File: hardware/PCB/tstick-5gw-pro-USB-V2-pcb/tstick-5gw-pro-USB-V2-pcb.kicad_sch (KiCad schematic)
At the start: 55 parts, among them J1 USB_C_Receptacle_USB2.0, J2 GPIO2, J3 GPIO1, Q3 BSS138, SW1 JST-SH-1.00mm 1x2, SW2 PTS810 SJM Switch, SW3 PTS810 SJM Switch, U1 max8819ceti+, U4 PCA9306DP

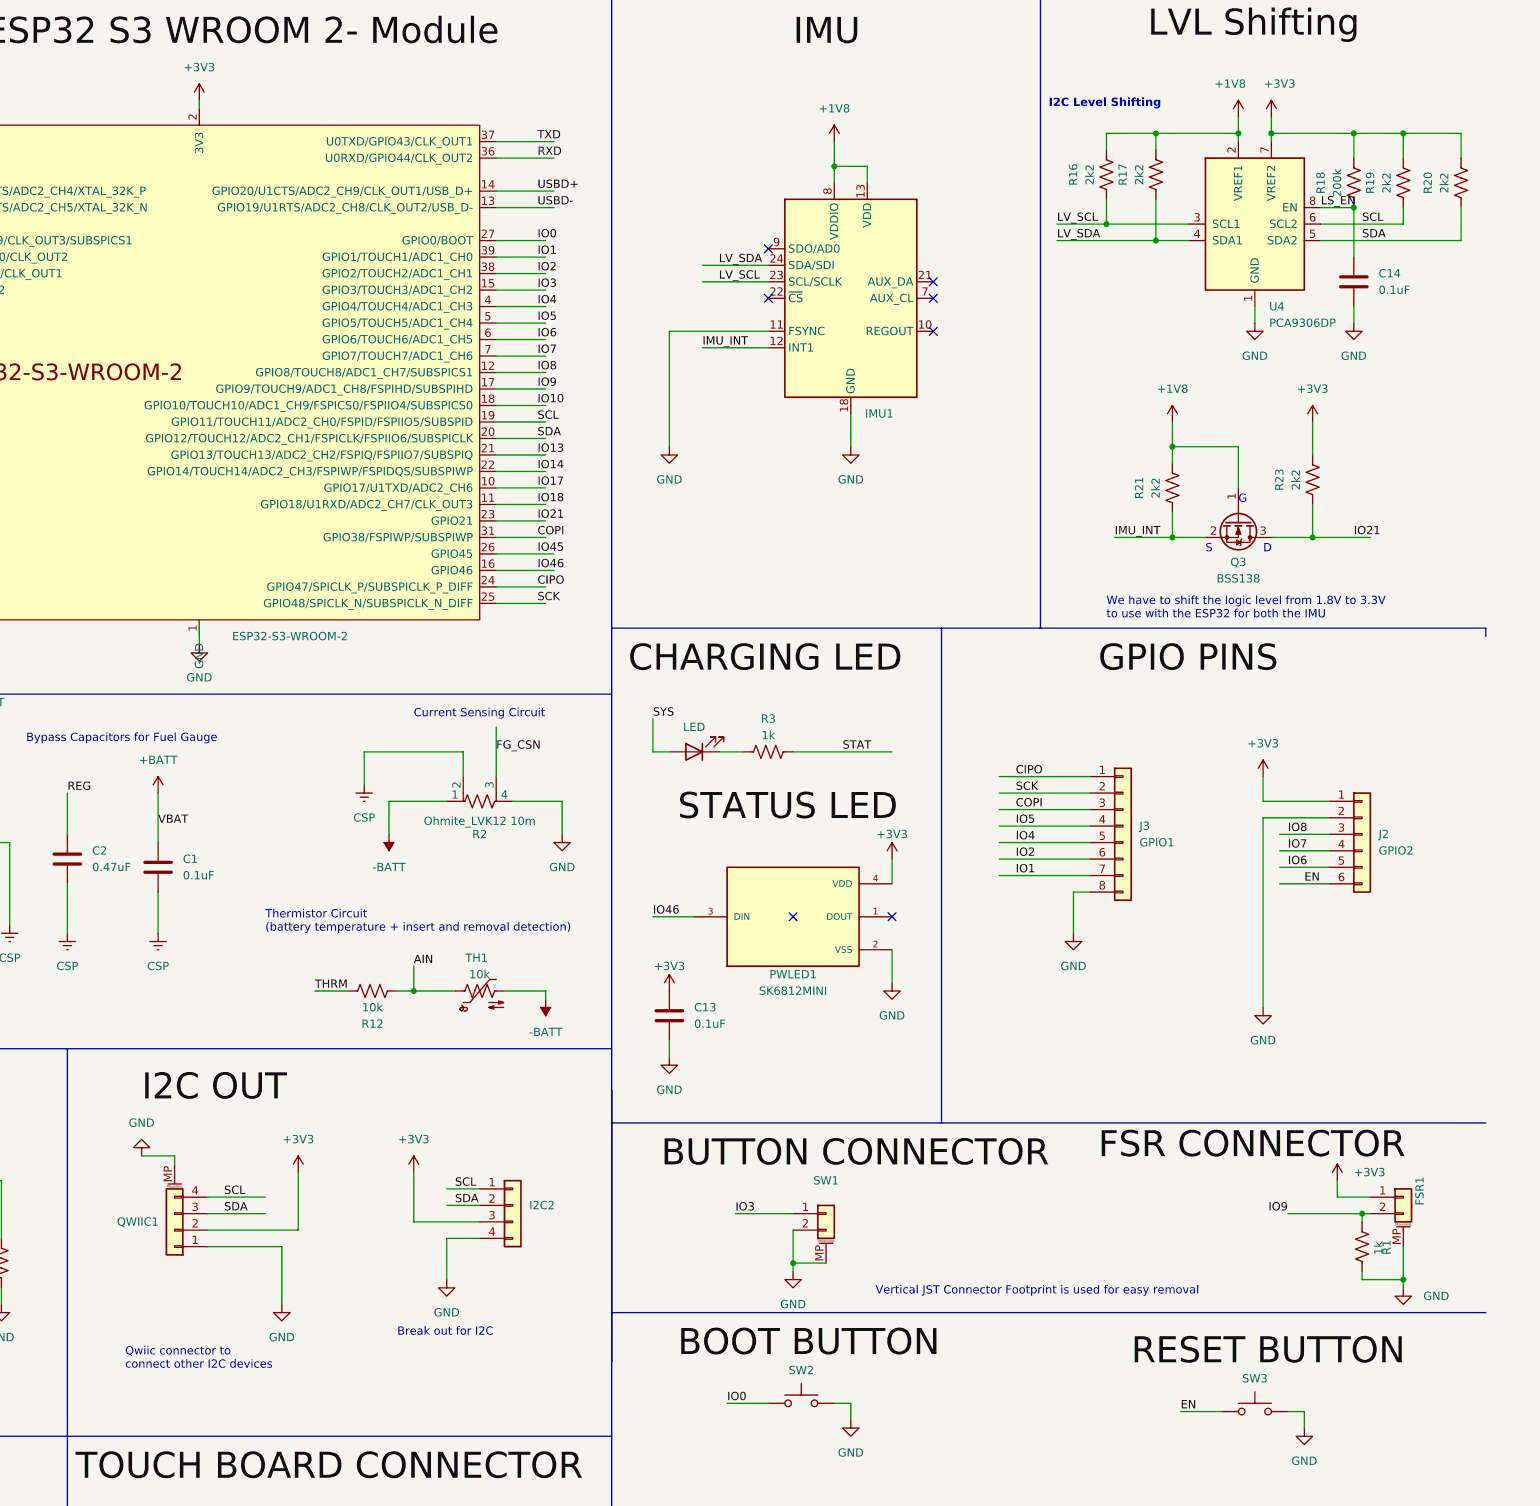
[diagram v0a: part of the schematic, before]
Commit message: cleaned up layout, board 1x2.2 inches, holes now 0.7 inch apart, lined up gpio holes
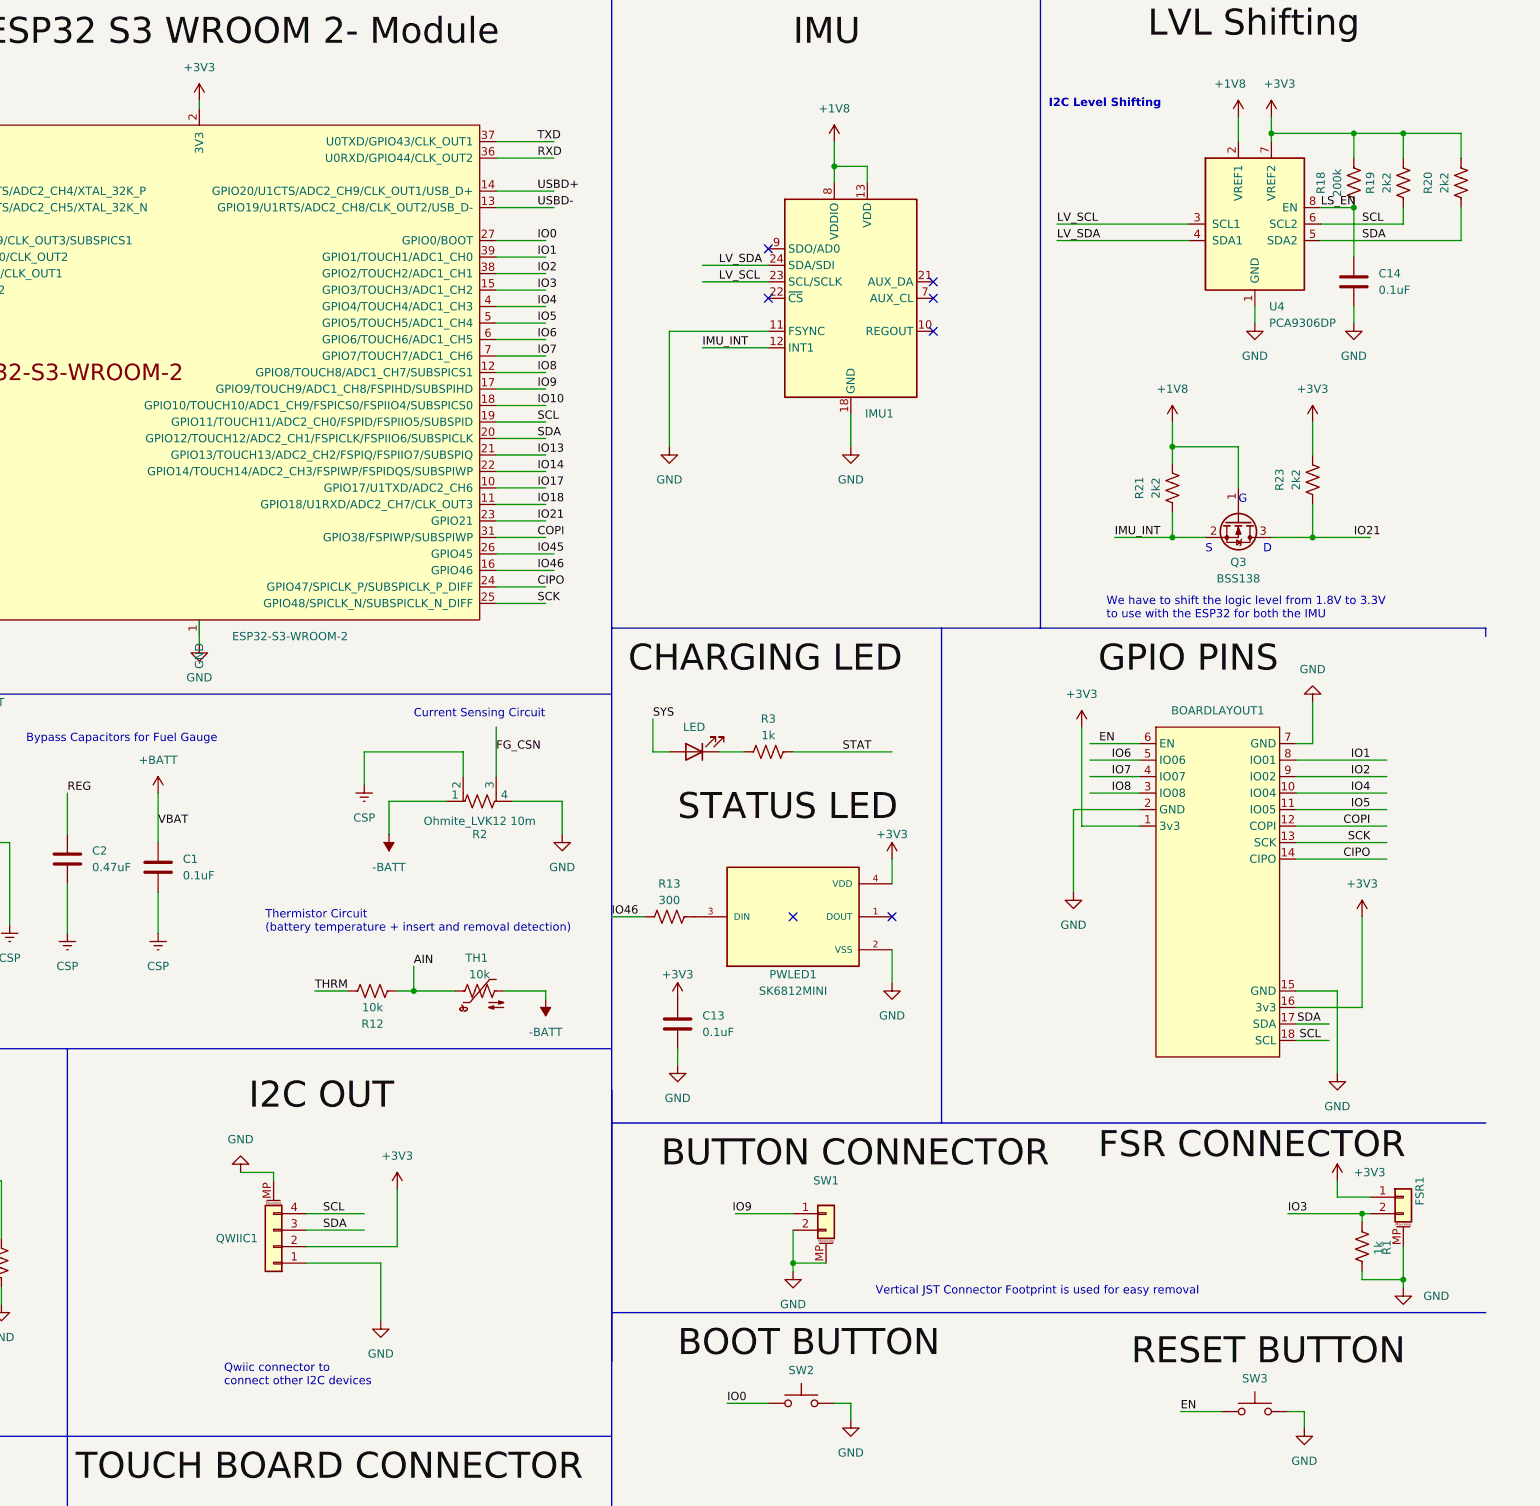
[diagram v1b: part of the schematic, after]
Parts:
- removed I2C2: Conn_01x04, Connector_PinHeader_2.54mm:PinHeader_2x02_P2.54mm_Vertical, symbol Connector_Generic:Conn_01x04
- removed J2: GPIO2, Connector_PinHeader_2.54mm:PinHeader_1x06_P2.54mm_Vertical, symbol Connector_Generic:Conn_01x06
- removed J3: GPIO1, Connector_PinHeader_2.54mm:PinHeader_1x08_P2.54mm_Vertical, symbol Connector_Generic:Conn_01x08
- removed R16, R17: 2k2, Resistor_SMD:R_0201_0603Metric, symbol Device:R_US
- added BOARDLAYOUT1: LAYOUT, pin-layout:board-layout, symbol pin-layout:board-layout
- added R13: 300, Resistor_SMD:R_0201_0603Metric, symbol Device:R_US
- SYS1, SYS2: now left out of the parts list
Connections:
- net +3V3: now also BOARDLAYOUT1.1 (3v3), BOARDLAYOUT1.16 (3v3)
- net CIPO: now also BOARDLAYOUT1.14 (CIPO)
- net COPI: now also BOARDLAYOUT1.12 (COPI)
- net EN: now also BOARDLAYOUT1.6 (EN)
- net GND: now also BOARDLAYOUT1.15 (GND), BOARDLAYOUT1.2 (GND), BOARDLAYOUT1.7 (GND)
- net IO1: now also BOARDLAYOUT1.8 (IO01)
- net IO2: now also BOARDLAYOUT1.9 (IO02)
- net IO3: now also FSR1.2 (Pin_2), R1.1; no longer SW1.1 (Pin_1)
- net IO4: now also BOARDLAYOUT1.10 (IO04)
- net IO46: now also R13.1; no longer PWLED1.3 (DIN)
- net IO5: now also BOARDLAYOUT1.11 (IO05)
- net IO6: now also BOARDLAYOUT1.5 (IO06)
- net IO7: now also BOARDLAYOUT1.4 (IO07)
- net IO8: now also BOARDLAYOUT1.3 (IO08)
- net IO9: now also SW1.1 (Pin_1); no longer FSR1.2 (Pin_2), R1.1
- net SCK: now also BOARDLAYOUT1.13 (SCK)
- net SCL: now also BOARDLAYOUT1.18 (SCL)
- net SDA: now also BOARDLAYOUT1.17 (SDA)
- new net: PWLED1.3 (DIN), R13.2
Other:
- note removed: "Break out for I2C"
- moved on the sheet: C13, QWIIC1

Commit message: added new version of trill craft breakout pcb using castellated pads
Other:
- note removed: "Based on Travis West Initial PCB Design for T-Stick"
- moved on the sheet: C4, L1, R18, R19, R20, R8, R9

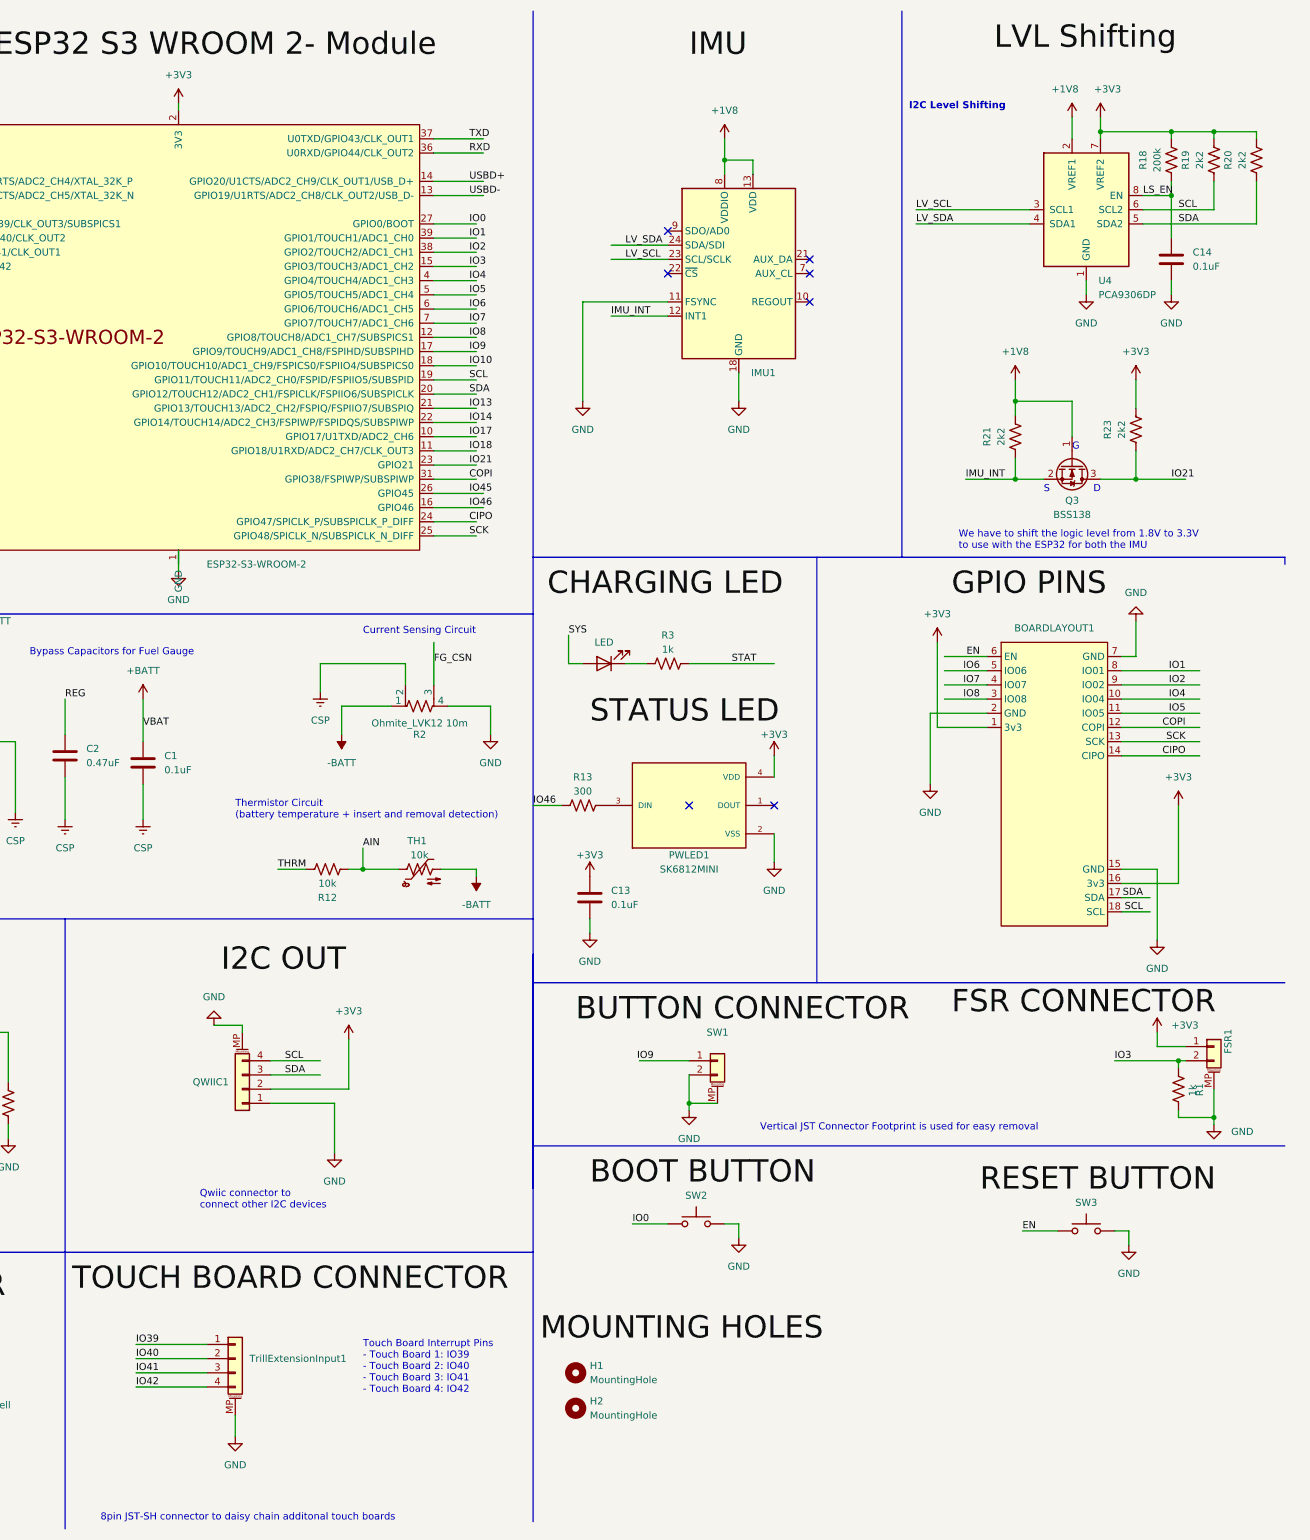
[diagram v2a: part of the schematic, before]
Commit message: fixed errors in schematic, added support for V1 Trill boards in v2 board design, changed headers to vertical headers in touch board
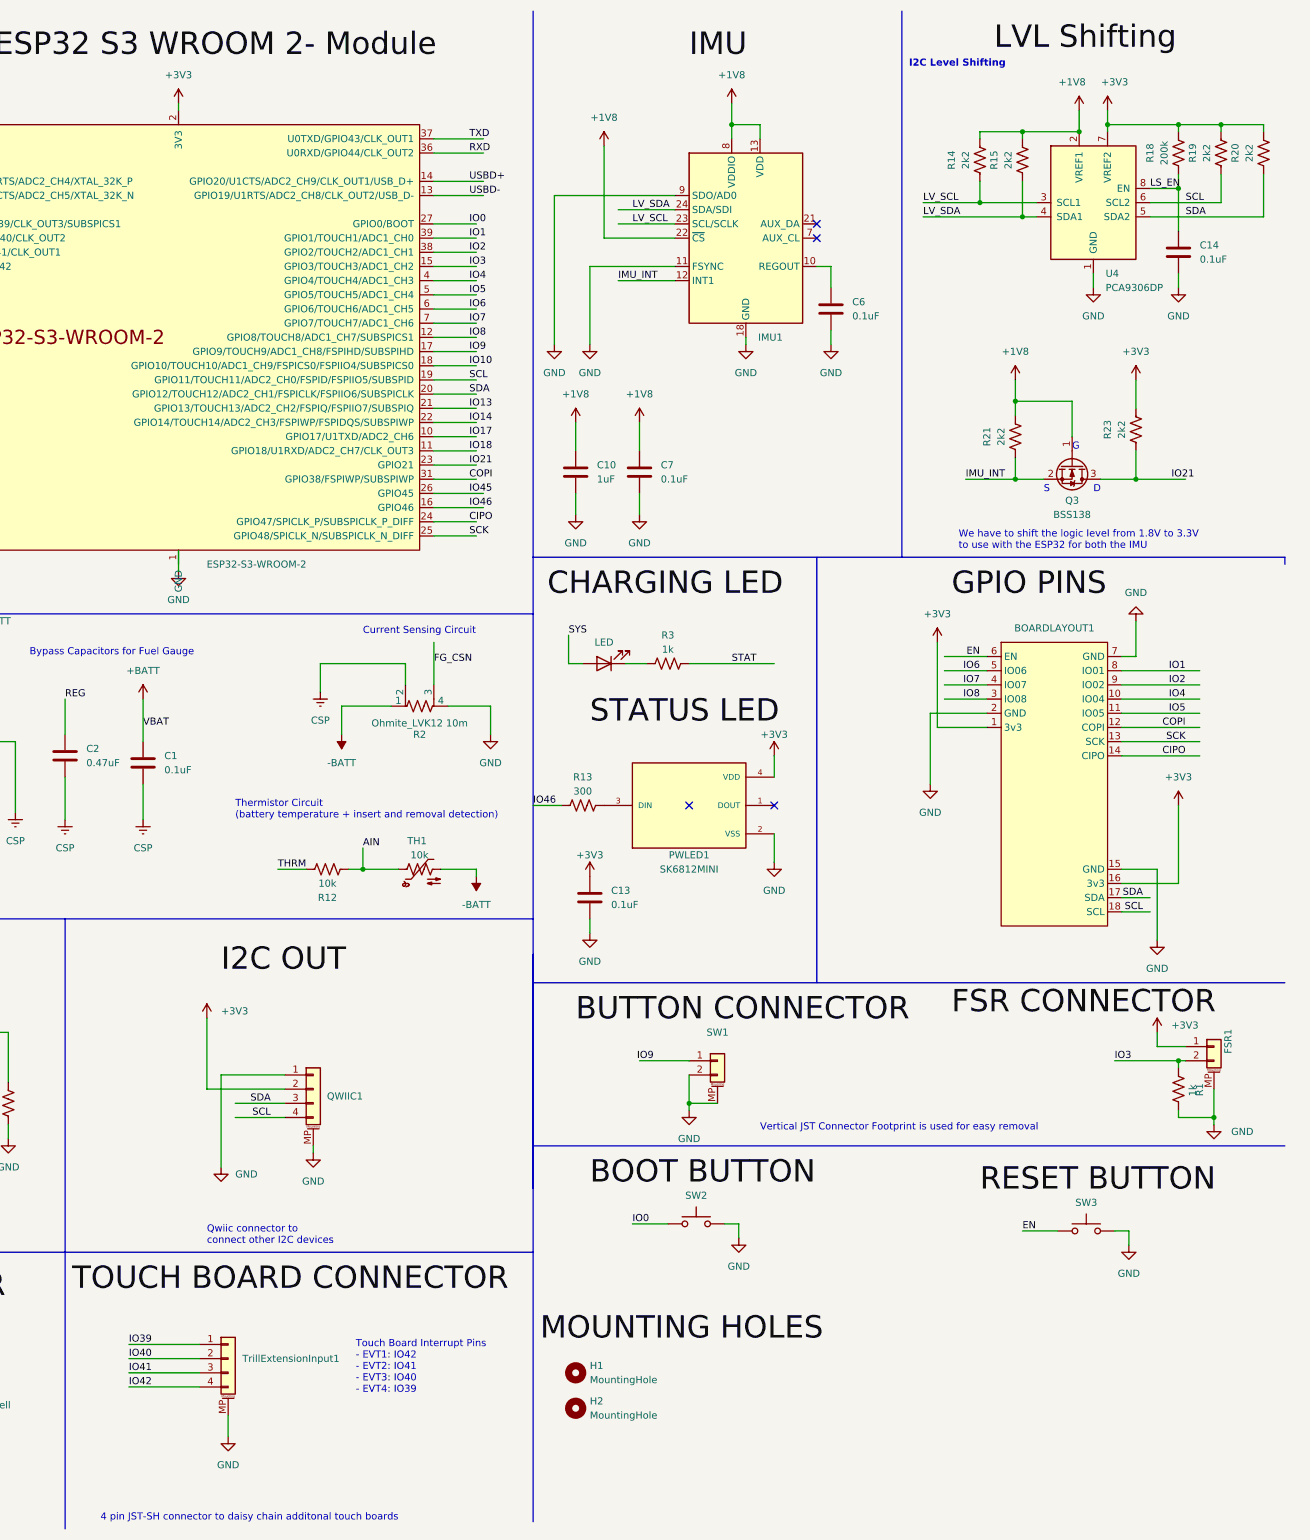
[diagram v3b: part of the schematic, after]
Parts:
- added C10: 1uF, Capacitor_SMD:C_0201_0603Metric, symbol Device:C
- added C6, C7: 0.1uF, Capacitor_SMD:C_0201_0603Metric, symbol Device:C
- added R14, R15: 2k2, Resistor_SMD:R_0201_0603Metric, symbol Device:R_US
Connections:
- net +1V8: now also IMU1.22 (~{CS}), C10.1, C7.1, R14.2, R15.2
- net GND: now also IMU1.9 (SDO/AD0), C10.2, C6.2, C7.2
- net LV_SCL: now also R14.1
- net LV_SDA: now also R15.1
- net at IMU1.10 (REGOUT): now also C6.1
- no-connect marks 11 -> 8
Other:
- note added: "4 pin JST-SH connector to daisy chain additonal touch boards"
- note added: "Touch Board Interrupt Pins - EVT1: IO42 - EVT2: IO41 - EVT3: IO40 - EVT4: IO39"
- note removed: "8pin JST-SH connector to daisy chain additonal touch boards"
- note removed: "Touch Board Interrupt Pins - Touch Board 1: IO39 - Touch Board 2: IO40 - Touch Board 3: IO41 - Touch Board 4: IO42"
- moved on the sheet: C14, IMU1, QWIIC1, R18, R19, R20, TrillExtensionInput1, U4
